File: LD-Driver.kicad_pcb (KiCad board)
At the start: 2 copper layers, 102.5 x 71.5 mm, 133 parts, among them J1 BASYS3, J3 Barrel_Jack_Switch, Q1 RJK0355DSP, Q10 RJK0355DSP, Q11 DMP3037LSS-13, Q2 RJK0355DSP, Q3 SiRC18DP, Q4 SiRC18DP, Q5 SiRC18DP, Q6 SiRC18DP, Q8 2N7002, Q9 RJK0355DSP, U1 MCP4728, U2 LM3743, U3 MAX1978, U4 INA333xxDGK, U5 MIC2101, U6 NCP1117-3.3_SOT223

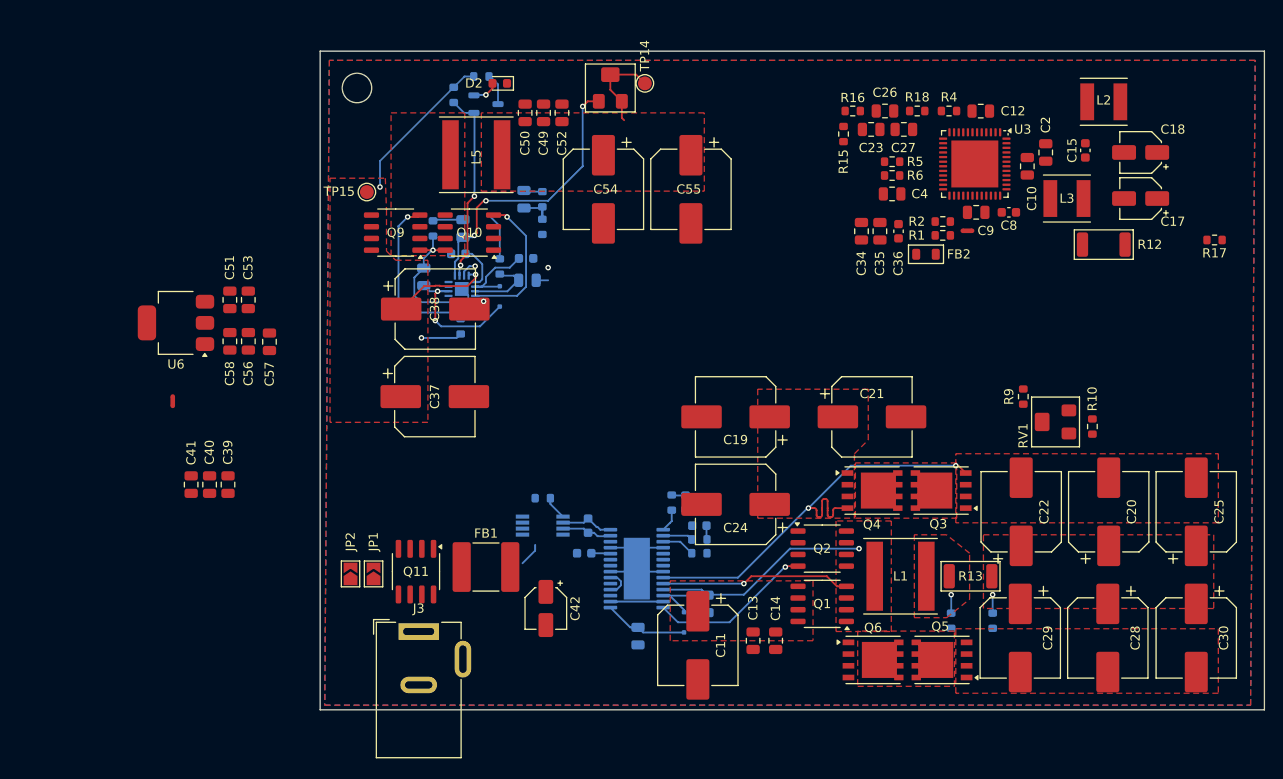
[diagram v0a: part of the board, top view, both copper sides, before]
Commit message: small schematic correction, structural changes to the 5V buck on the pcb
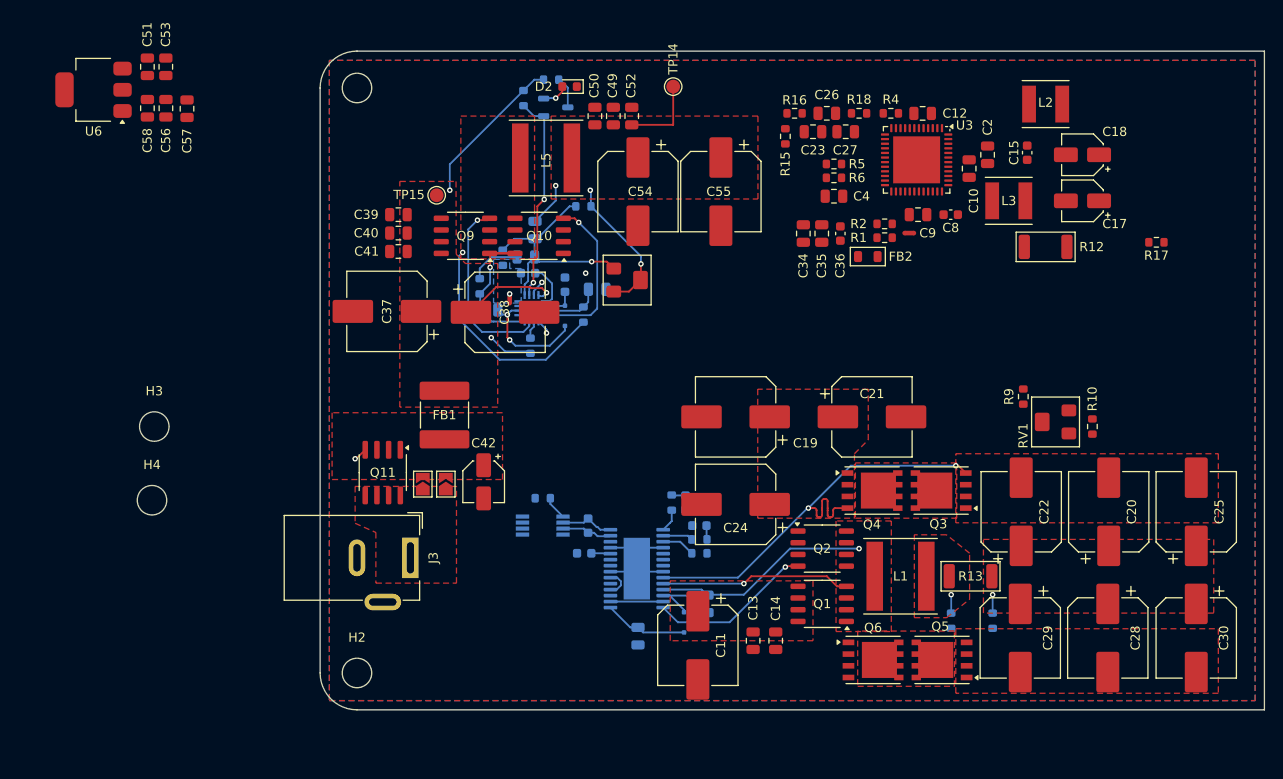
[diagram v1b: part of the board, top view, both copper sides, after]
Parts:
- removed REF**: MountingHole_3.2mm_M3_ISO7380, MountingHole:MountingHole_3.2mm_M3_ISO7380
- added H1: MountingHole, MountingHole:MountingHole_3.2mm_M3_ISO7380, F.Cu at (161.0, 35.0)
- added H2: MountingHole, MountingHole:MountingHole_3.2mm_M3_ISO7380, F.Cu at (161.0, 98.5)
- added H3: MountingHole, MountingHole:MountingHole_3.2mm_M3_ISO7380, F.Cu at (139.0, 71.8)
- added H4: MountingHole, MountingHole:MountingHole_3.2mm_M3_ISO7380, F.Cu at (138.8, 79.8)
- moved NT2 38.2 mm to (177.6, 57.8), turned to 90 degrees
- moved C39 34.7 mm to (165.5, 48.8), turned to 180 degrees
- moved C40 34.1 mm to (165.5, 50.8), turned to 180 degrees
- moved C41 33.9 mm to (165.5, 52.8), turned to 180 degrees
- moved C56 26.8 mm to (140.3, 37.2)
- moved C51 26.8 mm to (138.2, 32.7)
- moved C58 26.8 mm to (138.2, 37.2)
- moved U6 26.8 mm to (132.4, 35.2)
- moved C57 26.8 mm to (142.6, 37.2)
- moved C53 26.8 mm to (140.2, 32.7)
- moved RV2 20.9 mm to (190.3, 55.9), turned to 90 degrees
- moved FB1 17.1 mm to (170.5, 70.5), turned to 90 degrees
- moved C42 15.3 mm to (174.8, 77.8)
- moved JP1 12.5 mm to (170.6, 78.0)
- moved JP2 12.5 mm to (168.1, 78.0)
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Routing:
- net Net-(U5-SW): track 19.0 -> 41.0 mm, vias 1 -> 2
- net +5V: track 11.6 -> 31.7 mm, vias 0 -> 3
- net /Power/FB: track 35.7 -> 25.6 mm, vias 3 -> 1
- net Net-(D3-A): track 9.10 -> 4.45 mm
- net Net-(D3-K): track 15.6 -> 12.9 mm
- net Net-(R19-Pad1): track 2.57 -> 0.00 mm
- net Net-(C47-Pad2): track 3.37 -> 5.67 mm
- net /Power/DL: track 15.8 -> 18.0 mm
- net /Power/DH: track 18.7 -> 20.5 mm
- net Net-(Q8-G): track 21.0 -> 22.7 mm
- net Net-(U5-ILIM): track 7.54 -> 6.51 mm
- net VDC: track 31.9 -> 32.5 mm
- net GND1: track 0.38 -> 0.78 mm, vias 0 -> 1
- net GND: track 25.9 -> 26.0 mm, vias 2 -> 3
- added copper zone on B.Cu, net GND1
- added copper zone on F.Cu, net Net-(JP1-A)
- added copper zone on F.Cu, net Net-(JP1-B)
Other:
- outline, holes or cut-outs redrawn

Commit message: update PCB: fixed buck layout, concept layout for LD driver with LT3743
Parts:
- removed the C19 at (202.1, 70.7)
- removed the C21 at (216.9, 70.7)
- removed the C24 at (202.1, 80.2)
- removed the C25 at (252.1, 81.0)
- removed the C29 at (233.0, 94.7)
- added C1: 100n, Capacitor_SMD:C_0805_2012Metric, F.Cu at (177.3, 90.8)
- added C26: 330u, Capacitor_SMD:CP_Elec_8x10.5, F.Cu at (239.0, 89.2)
- added C34: 100n, Capacitor_SMD:C_0805_2012Metric, F.Cu at (177.2, 82.5)
- added J2: Conn_02x07_Counter_Clockwise, footprints:Butterfly_14pins_SMD, F.Cu at (336.2, 81.7)
- added R22: 10k, Resistor_SMD:R_0603_1608Metric, F.Cu at (185.1, 52.8)
- C12: renamed from C13; moved to B.Cu
- C14, C49, C50: moved to B.Cu
- C28: renamed from C31; moved to B.Cu
- C29: renamed from C32; moved to B.Cu
- C30: renamed from C33; moved to B.Cu
- C37: renamed from C39; moved to B.Cu
- C38: renamed from C40; moved to B.Cu
- C39: renamed from C41; moved to B.Cu
- C51: renamed from C52; moved to B.Cu
- J1: footprint Connector_PinHeader_2.54mm:PinHeader_2x08_P2.54mm_Horizontal -> Connector_PinHeader_2.54mm:PinHeader_2x07_P2.54mm_Horizontal
- R19, U4: moved to F.Cu
- TP13: footprint TestPoint:TestPoint_Pad_2.5x2.5mm -> TestPoint:TestPoint_Pad_1.0x1.0mm; moved to B.Cu
- U2: value LM3743 -> LT3743
- moved TP2 245.8 mm to (275.0, 51.0)
- moved TP4 191.9 mm to (240.5, 80.7)
- moved TP6 166.5 mm to (214.5, 67.8)
- moved TP5 151.2 mm to (199.0, 94.9)
- moved TP13 140.6 mm to (179.1, 53.8), turned to 180 degrees
- moved TP7 140.2 mm to (189.2, 98.0)
- moved TP8 133.5 mm to (184.2, 91.8)
- moved TP9 132.7 mm to (184.2, 89.0)
- moved C30 131.2 mm to (228.2, 80.5), turned to 90 degrees
- moved C28 128.2 mm to (225.2, 80.5), turned to 90 degrees
- moved C29 125.3 mm to (222.2, 80.4), turned to 90 degrees
- moved TP12 123.8 mm to (159.2, 91.2)
- moved C18 84.9 mm to (315.2, 86.3), turned to -90 degrees
- moved C19 83.7 mm to (320.0, 66.2), turned to 90 degrees
- moved L3 83.7 mm to (311.4, 72.5)
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- renumbered C9 to C10, C10 to C11, C12 to C13, C11 to C15, C15 to C16, C16 to C17, C17 to C18, C18 to C19, C1 to C2, C23 to C21, C26 to C23, C27 to C24, C28 to C25, C30 to C27, C2 to C3, C34 to C31, C35 to C32, C36 to C33, C37 to C35, C38 to C36, C3 to C4, C42 to C40, C43 to C41, C44 to C42, C45 to C43, C46 to C44, C47 to C45, C48 to C46, C51 to C47, C53 to C48, C4 to C5, C56 to C52, C54 to C53, C57 to C54, C58 to C56, C5 to C6, C6 to C7, C7 to C8, C8 to C9, FB2 to FB1, FB1 to FB2, L3 to L2, L2 to L3, L5 to L4, Q11 to Q7, R22 to R23, R23 to R24, R24 to R25, R25 to R26, R26 to R27
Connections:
- J1 pad 1: +5V -> /RDY/~{BSY}
- J1 pad 10: GND -> /UNDERTMP_ALM
- J1 pad 11: /SUPPLY_EN -> GND
- J1 pad 12: /SCL -> /OVERTMP_ALM
- J1 pad 13: /SDA -> /TEC_EN
- J1 pad 14: /~{LDAC} -> /ITEC_MON
- J1 pad 2: /OVERTMP_ALM -> /LD_MOD
- J1 pad 3: /UNDERTMP_ALM -> /~{LDAC}
- J1 pad 4: /ITEC_MON -> /CTRL_SEL
- J1 pad 5: /ILD_MON_ADC -> /SDA
- J1 pad 6: /LD_MOD -> /ILD_MON
- J1 pad 7: /TEC_EN -> /SCL
- Q4 pad 1: Net-(C19-Pad1) -> GND
- Q4 pad 2: Net-(C19-Pad1) -> GND
- Q4 pad 3: Net-(C19-Pad1) -> GND
- U1 pad 6: /Driver/MAXV_DAC -> /Driver/CTRL_L_DAC
- U1 pad 8: /Driver/CTRL_L_DAC -> /Driver/MAXV_DAC
- U5 pad 15: /SUPPLY_EN -> Net-(U5-EN)
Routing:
- net /Driver/PWMGH: track 0.00 -> 37.8 mm, vias 0 -> 2
- net /Driver/SENSE+: track 5.51 -> 37.4 mm, vias 0 -> 1
- net /Driver/SENSE-: track 5.84 -> 36.7 mm, vias 0 -> 1
- net /LD_MOD: track 0.00 -> 27.5 mm, vias 0 -> 1
- net /CTRL_SEL: track 0.00 -> 25.8 mm, vias 0 -> 1
- net /LD_EN: track 3.07 -> 27.5 mm, vias 0 -> 2
- net GND: track 26.0 -> 49.7 mm, vias 3 -> 32
- net /ILD_MON: track 0.00 -> 22.7 mm, vias 0 -> 2
- net +3V3: track 0.00 -> 21.6 mm
- net /Power/FB: track 25.6 -> 41.7 mm
- net /Driver/CTRL_H_DAC: track 0.00 -> 16.0 mm, vias 0 -> 1
- net /Driver/SW: track 23.6 -> 9.27 mm
- net /Driver/PWMGL: track 47.7 -> 34.2 mm, vias 2 -> 3
- net Net-(Q2-G): track 17.8 -> 4.52 mm
- net /Driver/CTRL_L_DAC: track 0.00 -> 12.7 mm, vias 0 -> 1
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- removed copper zone on F.Cu, net Net-(C19-Pad1)

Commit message: Changed overall subsystem positions, TEC controller implemented, LD controller IC position to be reconsidered in order to have enough clearance after header connector is fully routed
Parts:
- removed C47, C54, C56: 10u, Capacitor_SMD:C_0805_2012Metric
- removed C48, C52: 100n, Capacitor_SMD:C_0805_2012Metric
- removed U6: NCP1117-3.3_SOT223, Package_TO_SOT_SMD:SOT-223-3_TabPin2
- added NT3: NetTie_2, NetTie:NetTie-2_SMD_Pad0.5mm, B.Cu at (128.3, 130.7)
- C10, C13, C3, C31, C32, C33, C34, FB1, R1, R19, R2, U4: moved to B.Cu
- TP1, TP11: footprint TestPoint:TestPoint_Pad_D1.5mm -> TestPoint:TestPoint_Pad_D1.0mm
- moved R10 248.1 mm to (50.0, 61.0)
- moved R9 234.6 mm to (55.0, 63.0), turned to 0 degrees
- moved RV1 222.0 mm to (75.2, 57.1), turned to 180 degrees
- moved R17 201.1 mm to (125.5, 115.2), turned to -90 degrees
- moved C11 195.3 mm to (115.1, 114.8)
- moved C19 192.9 mm to (128.4, 89.1), turned to 180 degrees
- moved J2 192.6 mm to (145.4, 107.7)
- moved R18 192.0 mm to (104.4, 103.7), turned to -90 degrees
- moved C18 191.4 mm to (128.1, 126.8), turned to 180 degrees
- moved C23 189.5 mm to (104.8, 106.2), turned to 0 degrees
- moved L2 189.4 mm to (121.8, 121.0)
- moved R12 188.9 mm to (129.4, 121.2)
- moved C16 188.8 mm to (124.2, 103.7)
- moved C3 188.5 mm to (120.7, 105.1), turned to 0 degrees
- moved R5 187.9 mm to (108.5, 113.8), turned to 90 degrees
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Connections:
- U3 pad 2: Net-(U3-NC-Pad2) -> unconnected-(U3-NC-Pad2)
- U3 pad 29: Net-(U3-NC-Pad2) -> unconnected-(U3-NC-Pad29)
- U3 pad 35: Net-(U3-NC-Pad2) -> unconnected-(U3-NC-Pad35)
- U3 pad 49: (no net) -> GND
- U3 pad 8: Net-(U3-NC-Pad2) -> unconnected-(U3-NC-Pad8)
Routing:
- net /Driver/FB+: track 0.00 -> 71.7 mm, vias 0 -> 4
- net /Driver/NTC+: track 0.00 -> 46.9 mm, vias 0 -> 6
- net /Driver/LD: track 7.72 -> 50.9 mm
- net +5V: track 29.3 -> 70.8 mm, vias 5 -> 9
- net Net-(L2-Pad1): track 0.00 -> 33.9 mm
- net /Driver/INTOUT: track 0.00 -> 27.5 mm, vias 0 -> 2
- net GNDA: track 0.00 -> 26.0 mm, vias 0 -> 6
- net /LD_MOD: track 27.5 -> 2.05 mm
- net /CTRL_SEL: track 25.8 -> 1.16 mm
- net /Driver/TEC+: track 0.00 -> 23.9 mm
- net /LD_EN: track 27.5 -> 3.83 mm, vias 2 -> 0
- net Net-(L3-Pad1): track 0.00 -> 23.2 mm
- net /ILD_MON: track 22.7 -> 0.00 mm, vias 2 -> 0
- net +1V5: track 0.00 -> 22.5 mm, vias 0 -> 3
- net Net-(U3-CS): track 0.00 -> 22.1 mm
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- added copper zone on F.Cu, net /Driver/TEC+
- added copper zone on F.Cu, net /Driver/TEC-
- added copper zone on B.Cu, net GNDA
- added copper zone on F.Cu, net GNDA
- added copper zone on F.Cu, net Net-(L2-Pad1)
- added copper zone on F.Cu, net Net-(L3-Pad1)
- added copper zone on F.Cu, net Net-(U3-CS)
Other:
- board size 102.5 x 71.5 mm -> 99 x 80 mm

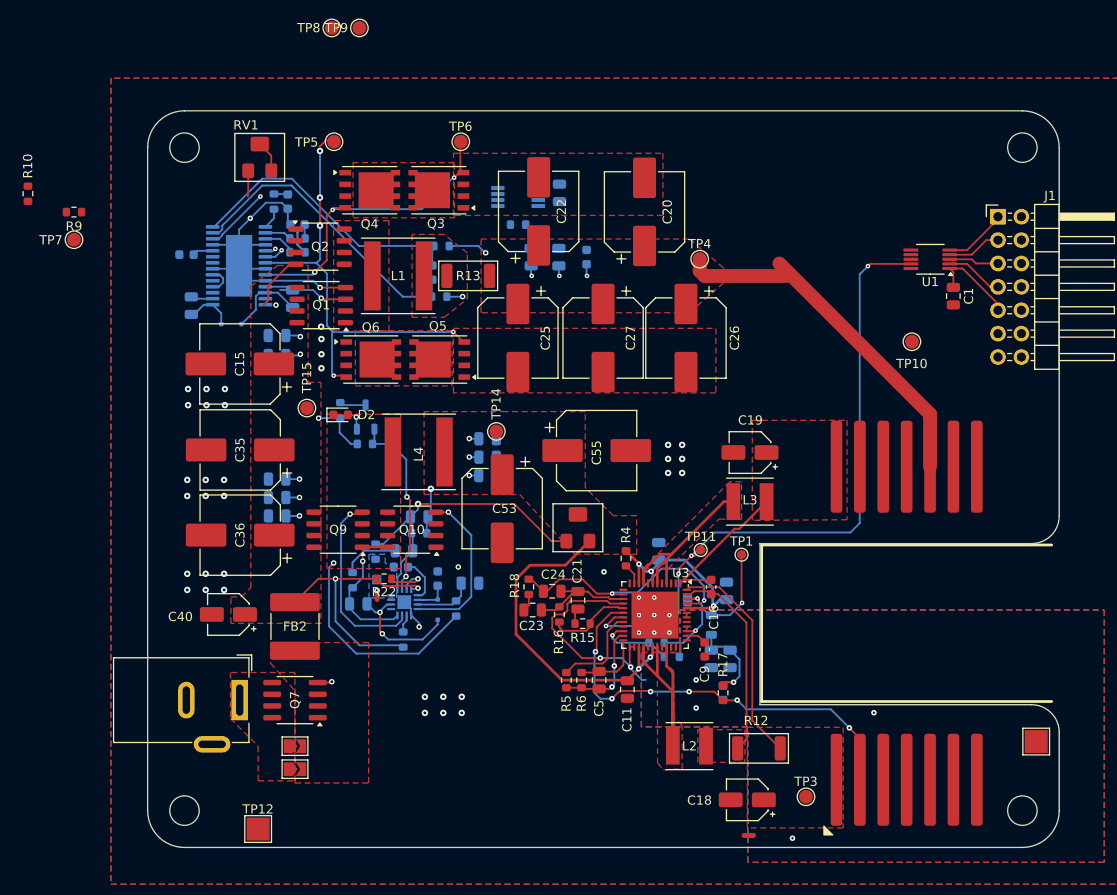
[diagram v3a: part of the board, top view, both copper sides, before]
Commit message: PCB routing completed, started uniforming components for smaller BOM
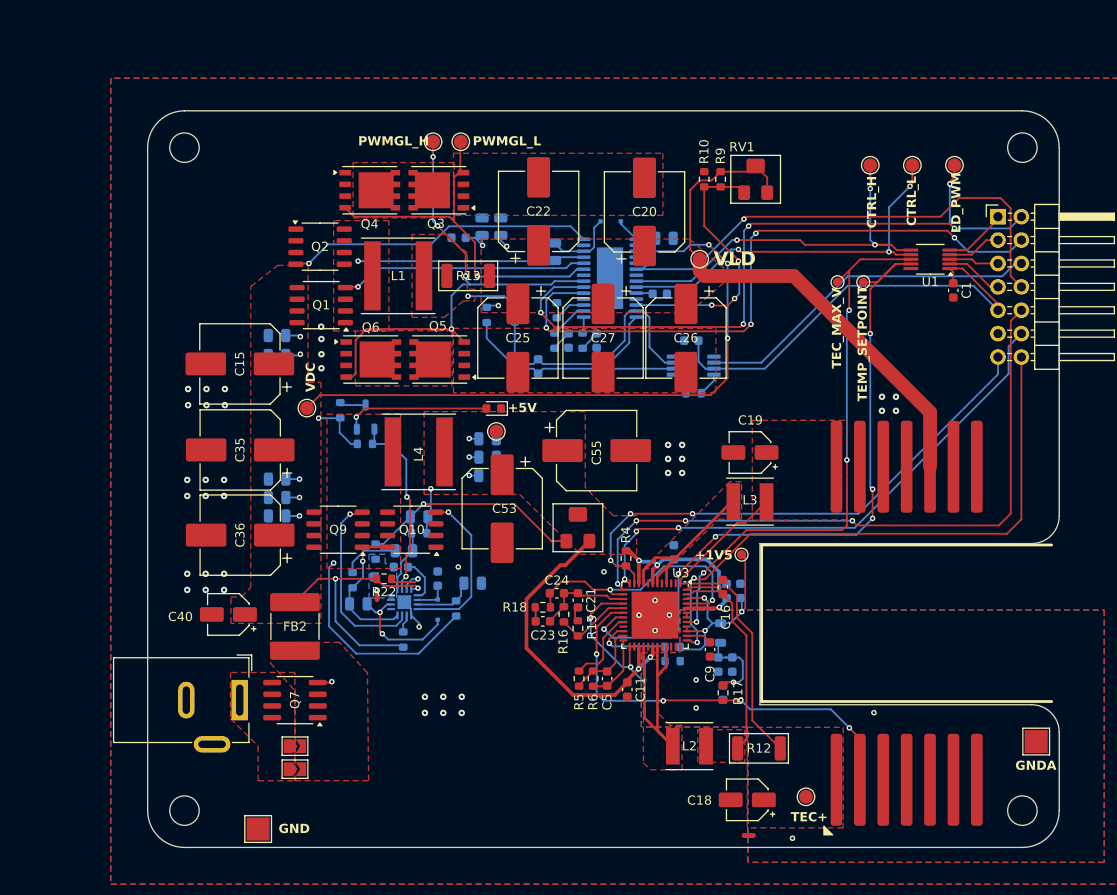
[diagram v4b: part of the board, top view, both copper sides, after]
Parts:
- C1, C10, C11, C13, C21, C23, C24, C3, C31, C32, C34, C5: footprint Capacitor_SMD:C_0805_2012Metric -> Capacitor_SMD:C_0603_1608Metric
- TP10: footprint TestPoint:TestPoint_Pad_D1.5mm -> TestPoint:TestPoint_Pad_D1.0mm
- moved TP7 96.0 mm to (150.6, 57.9)
- moved R10 73.5 mm to (123.4, 59.4)
- moved R9 70.3 mm to (125.2, 59.4), turned to 90 degrees
- moved TP9 61.9 mm to (146.1, 57.9)
- moved TP8 60.3 mm to (141.5, 57.9)
- moved RV1 53.9 mm to (129.0, 59.4)
- moved C8 51.9 mm to (119.1, 65.8), turned to 180 degrees
- moved C2 51.6 mm to (118.6, 71.9), turned to 180 degrees
- moved D1 42.7 mm to (113.3, 64.0), turned to 0 degrees
- moved U2 40.3 mm to (113.2, 70.2), turned to 180 degrees
- moved C6 36.8 mm to (111.8, 77.0)
- moved R7 36.8 mm to (110.2, 77.0), turned to -90 degrees
- moved TP11 34.0 mm to (140.7, 70.6)
- moved C7 32.0 mm to (108.7, 77.0), turned to 90 degrees
- moved R8 30.0 mm to (107.2, 77.0), turned to -90 degrees
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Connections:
- U1 pad 6: /Driver/CTRL_L_DAC -> /Driver/CTRL_H_DAC
- U1 pad 7: /Driver/CTRL_H_DAC -> /Driver/CTRL_L_DAC
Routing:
- net /LD_MOD: track 2.05 -> 78.0 mm, vias 1 -> 5
- net /UNDERTMP_ALM: track 0.00 -> 72.6 mm, vias 0 -> 4
- net VDC: track 42.9 -> 113.4 mm, vias 8 -> 11
- net /CTRL_SEL: track 1.16 -> 70.6 mm, vias 1 -> 4
- net /ITEC_MON: track 0.00 -> 64.6 mm, vias 0 -> 2
- net /Driver/MAXV_DAC: track 0.00 -> 61.2 mm, vias 0 -> 4
- net /OVERTMP_ALM: track 0.00 -> 58.9 mm, vias 0 -> 3
- net /TEC_EN: track 2.27 -> 58.2 mm, vias 0 -> 3
- net /LD_EN: track 3.83 -> 55.6 mm, vias 0 -> 1
- net /Driver/CTRL_H_DAC: track 0.00 -> 42.7 mm, vias 0 -> 3
- net /Driver/CTRL_L_DAC: track 0.00 -> 42.2 mm, vias 0 -> 3
- net +3V3: track 9.73 -> 49.2 mm
- net /ILD_MON: track 0.00 -> 37.9 mm
- net GND: track 39.8 -> 4.92 mm, vias 47 -> 46
- net Net-(Q2-G): track 6.30 -> 34.2 mm
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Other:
- board text added: "+1V5"
- board text added: "+5V"
- board text added: "CTRL_H"
- board text added: "CTRL_L"
- board text added: "GND"
- board text added: "GNDA"
- board text added: "LD_PWM"
- board text added: "PWMGL_H"
- board text added: "PWMGL_L"
- board text added: "TEC+"
- board text added: "TEC_MAX_V"
- board text added: "TEMP_SETPOINT"
- board text added: "VDC"
- board text added: "VLD"
